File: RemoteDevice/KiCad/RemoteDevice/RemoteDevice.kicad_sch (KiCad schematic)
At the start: 56 parts, among them J1 pin, J2 pin, Q1 PJA3411, Q2 PJA3411, SW1 BP, SW2 BP, U1 XC9140, U10 XBEE-3, U2 STM32L041F6Px, U3 MCP6281, U4 ADT7410TRZ, U5 MCP6281, U6 RT606, U7 Microphone, U8 LD2981CU33, U9 Con_4pts

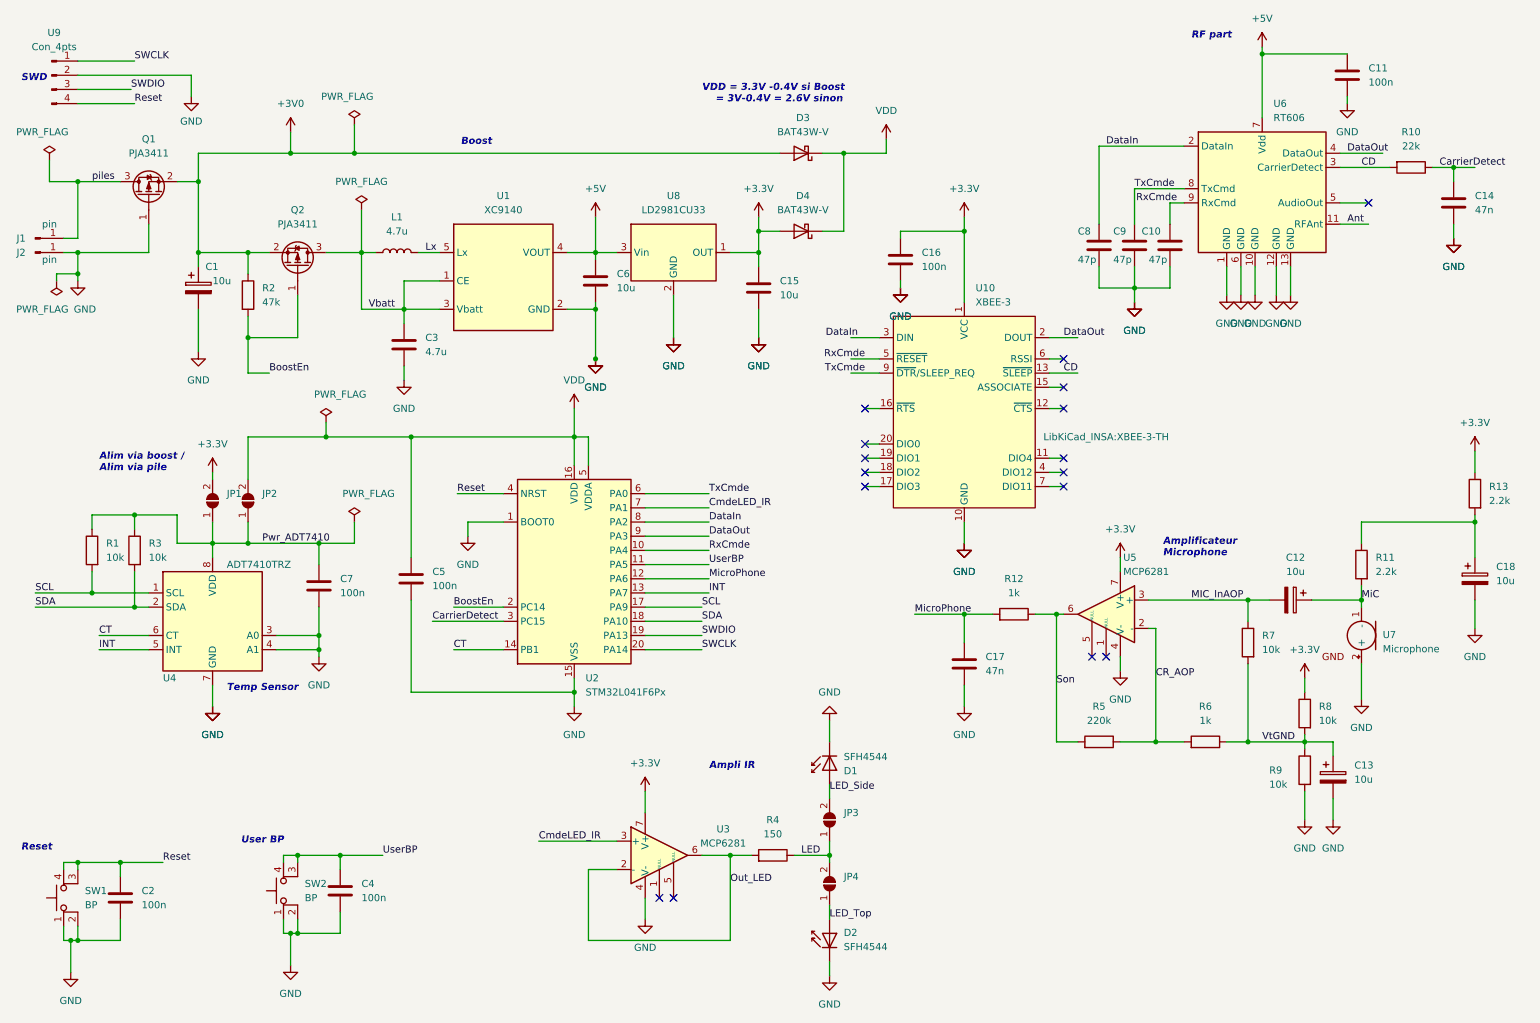
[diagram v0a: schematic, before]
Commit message: refonte du répertoire. Révision complète SySML pour y inclure la notion de Gateway et de SystemManager (Raspberry pi et touch screen). Revoir le protocole RDG en profondeur selon SysML à faire en premier
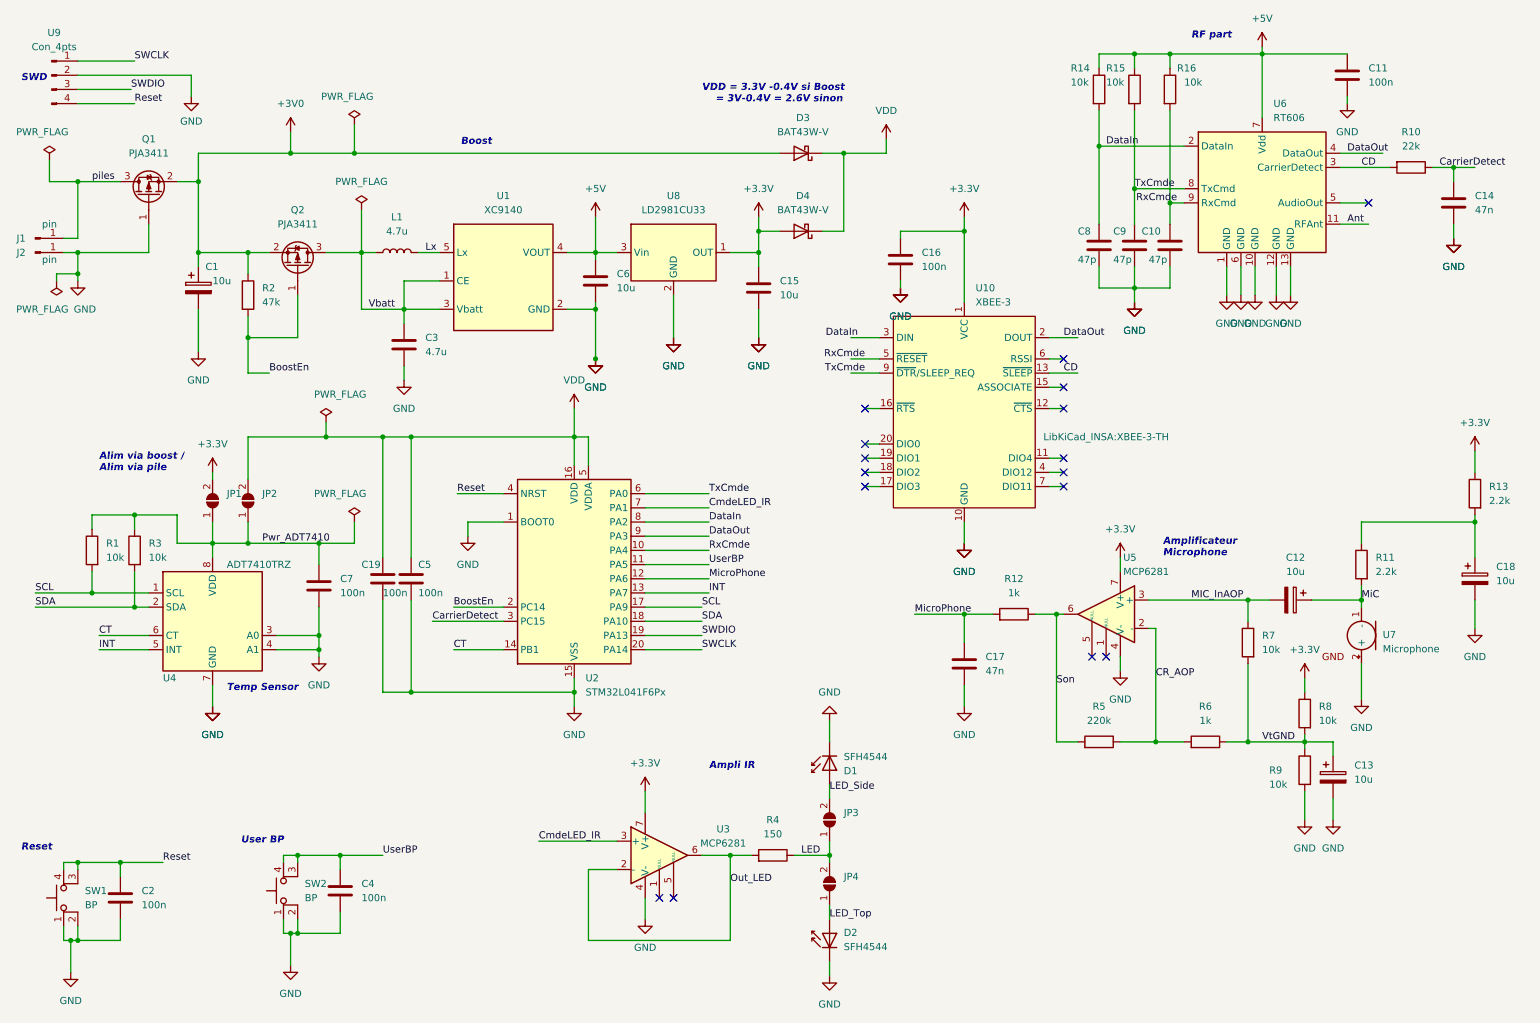
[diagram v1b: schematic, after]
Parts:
- added C19: 100n, Capacitor_SMD:C_1206_3216Metric, symbol Device:C
- added R14, R15, R16: 10k, Resistor_SMD:R_1206_3216Metric, symbol Device:R
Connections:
- net +5V: now also R14.1, R15.1, R16.1
- net DataIn: now also R14.2
- net GND: now also C19.2
- net RxCmde: now also R16.2
- net TxCmde: now also R15.2
- net VDD: now also C19.1
